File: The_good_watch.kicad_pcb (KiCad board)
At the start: 2 copper layers, 45 x 45 mm, 53 parts, among them IC1 DW01A, J1 Main, J2 USB_C_Receptacle_USB2.0, J3 PROG, J4 Screen, J5 Button, J6 Conn_02x07_Counter_Clockwise, M1 Motor_DC, Q1 FS8205A, Q2 LP0404N3T5G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

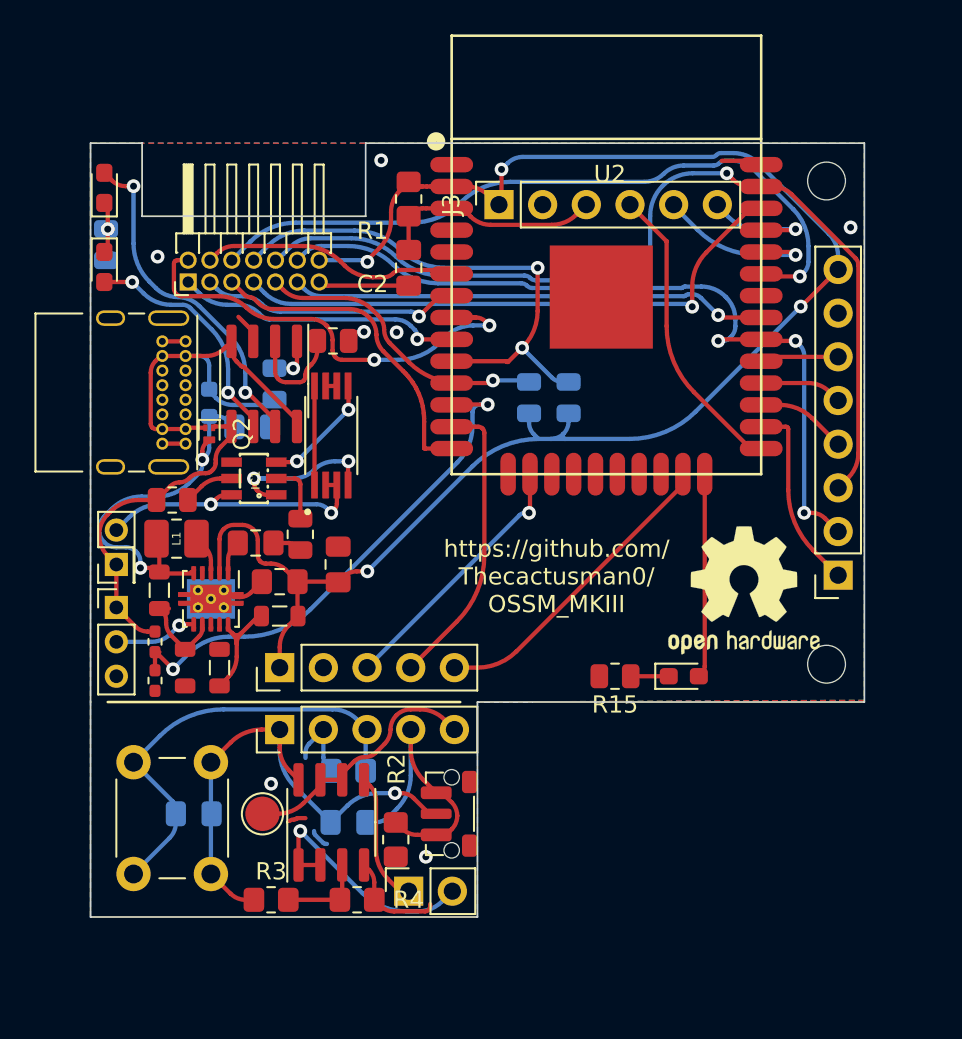
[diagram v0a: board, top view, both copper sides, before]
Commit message: Fixed more connector problems
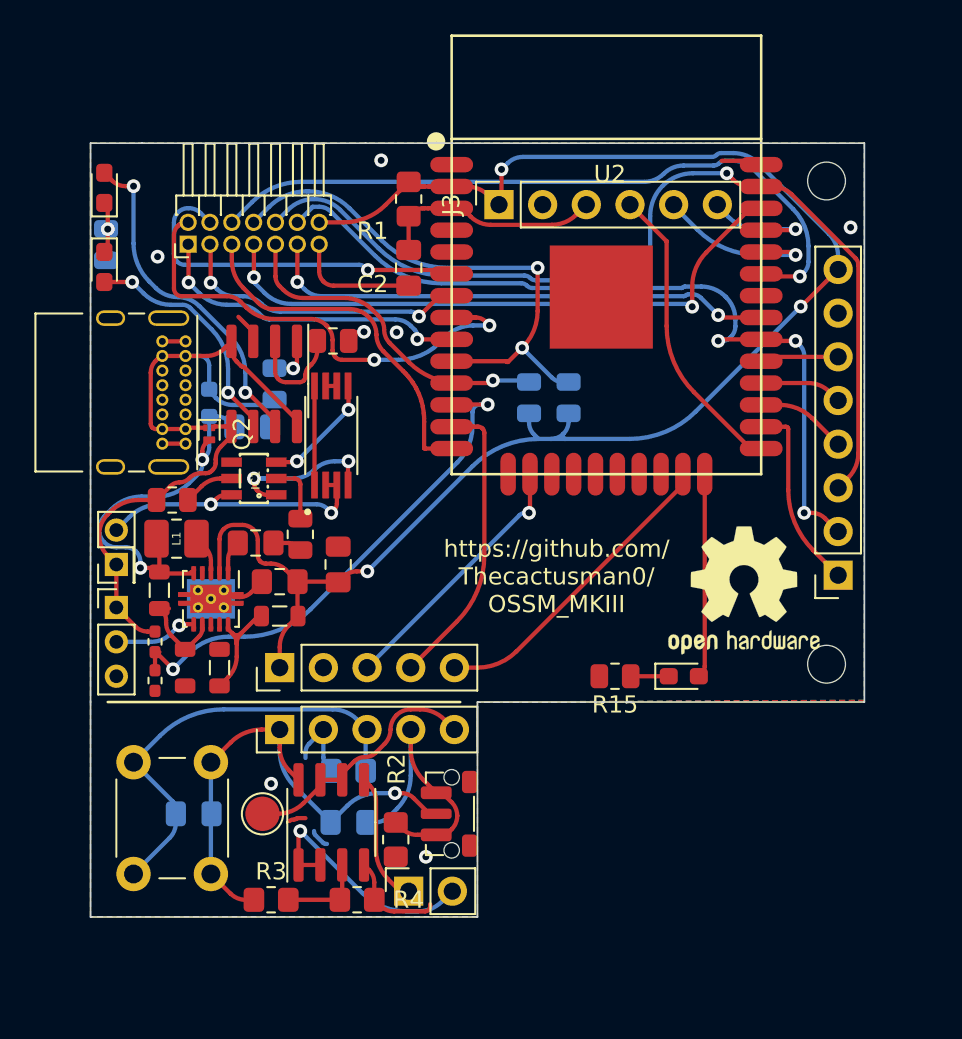
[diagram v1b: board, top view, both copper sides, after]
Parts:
- moved J6 2.20 mm to (105.7, 55.9)
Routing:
- net ANALOG2: track 15.0 -> 21.4 mm, vias 0 -> 1
- net ANALOG1: track 15.1 -> 17.4 mm, vias 1 -> 2
- net SENSE: track 16.7 -> 19.0 mm, vias 1 -> 2
- net MISO: track 27.8 -> 30.0 mm, vias 1 -> 2
- net MGPIO2: track 33.6 -> 35.8 mm, vias 1 -> 2
- net SCL: track 17.3 -> 19.5 mm
- net ANALOG0: track 27.4 -> 29.4 mm
- net GND: track 31.2 -> 33.2 mm
- net MGPIO0: track 18.9 -> 20.8 mm
- net +3V3: track 127.3 -> 125.8 mm, vias 5 -> 4
- net SCK: track 46.4 -> 47.5 mm
- net MOSI: track 55.2 -> 56.2 mm
- net SDA: track 30.4 -> 31.3 mm
- net MGPIO1: track 42.0 -> 41.4 mm
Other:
- outline, holes or cut-outs redrawn

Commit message: Fixed analog pins
encoder pins shut down when wifi enabled now fixed
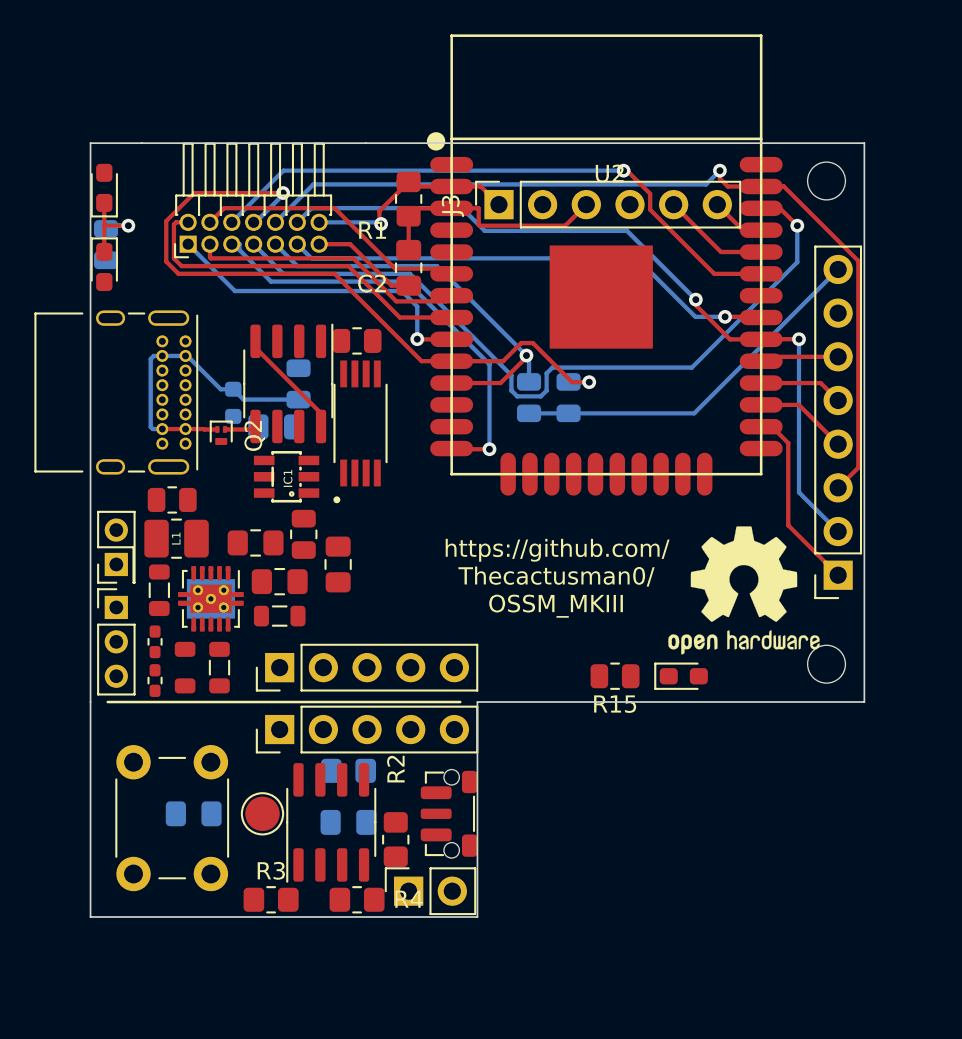
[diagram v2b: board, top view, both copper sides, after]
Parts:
- moved IC1 1.90 mm to (111.4, 69.4)
- moved Q1 1.84 mm to (115.7, 66.3)
- moved R7 1.40 mm to (115.5, 61.5)
- moved U3 1.40 mm to (111.5, 64.0)
- moved C7 1.40 mm to (110.8, 66.5)
- moved D4 1.40 mm to (108.3, 65.1)
- moved R19 1.40 mm to (112.1, 64.0)
- moved Q2 0.71 mm to (107.6, 67.0)
- moved R8 0.20 mm to (112.4, 72.8)
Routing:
- net +3V3: track 125.8 -> 34.6 mm, vias 4 -> 1
- net IO27: track 30.2 -> 0.00 mm, vias 2 -> 0
- net GND: track 33.2 -> 6.20 mm, vias 8 -> 0
- net B2: track 25.8 -> 0.00 mm
- net PSU: track 22.7 -> 0.00 mm, vias 2 -> 0
- net Net-(D2-Pad2): track 19.8 -> 0.00 mm, vias 2 -> 0
- net M_OUT_M: track 18.1 -> 0.00 mm
- net B1_M: track 17.9 -> 0.00 mm
- net +BATT: track 19.7 -> 1.84 mm
- net B1: track 17.4 -> 0.00 mm
- net IO0: track 17.4 -> 0.00 mm
- net -BATT: track 16.9 -> 0.00 mm, vias 2 -> 0
- net B2_M: track 15.4 -> 0.00 mm, vias 1 -> 0
- net M_OUT: track 14.5 -> 0.00 mm
- net Net-(M1-Pad2): track 14.3 -> 0.00 mm, vias 1 -> 0
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- removed copper zone on B.Cu, net GND
- removed copper zone on F.Cu, net GND

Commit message: Added diode protection on usb pwr in and redid layout
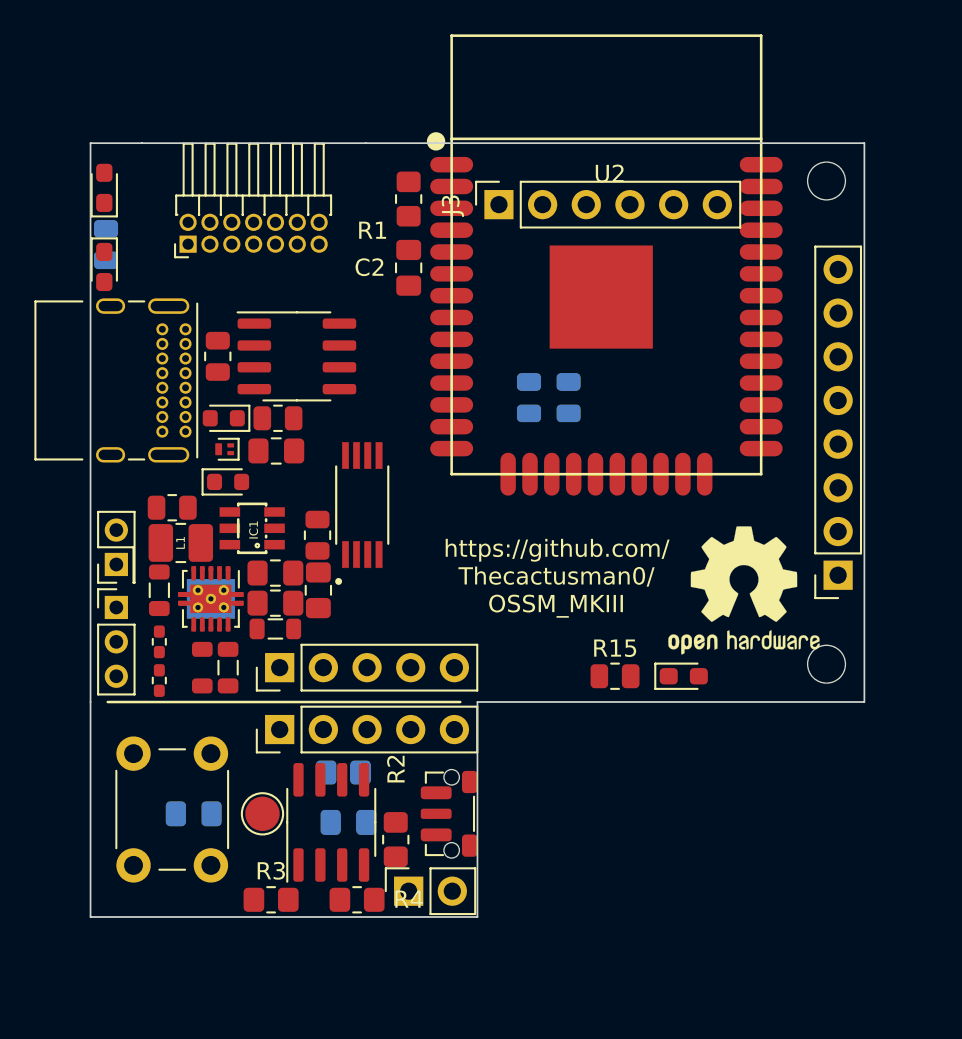
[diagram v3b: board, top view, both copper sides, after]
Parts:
- added D5: D_Schottky, Diode_SMD:D_0603_1608Metric, F.Cu at (107.8, 66.0)
- C7, D4, R19: moved to F.Cu
- moved R7 8.15 mm to (107.4, 62.4), turned to -90 degrees
- moved Q1 4.75 mm to (115.8, 71.0)
- moved D4 4.61 mm to (108.0, 69.7), turned to 0 degrees
- moved IC1 3.61 mm to (109.4, 72.4)
- moved R19 2.33 mm to (110.9, 66.0), turned to 180 degrees
- moved C4 2.09 mm to (110.8, 75.0)
- moved C3 1.89 mm to (113.2, 76.0)
- moved U3 1.68 mm to (112.0, 62.4), turned to 0 degrees
- moved C7 1.40 mm to (110.8, 67.9)
- moved C1 1.27 mm to (110.8, 76.8)
- moved R10 1.00 mm to (106.5, 80.5)
- moved Q2 0.82 mm to (107.8, 67.8), turned to 180 degrees
- moved R8 0.80 mm to (113.2, 72.8)
- moved R11 0.79 mm to (110.8, 78.2)
- moved J2 0.70 mm to (105.5, 60.8)
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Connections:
- J2 pad A4: VCC_IN -> Net-(J2-PadA4)
- J2 pad A9: VCC_IN -> Net-(J2-PadA4)
- J2 pad B4: VCC_IN -> Net-(J2-PadA4)
- J2 pad B9: VCC_IN -> Net-(J2-PadA4)
- J6 pad 2: ANALOG0 -> MGPIO0
- J6 pad 3: ANALOG1 -> MGPIO1
- J6 pad 4: ANALOG2 -> MGPIO2
- J6 pad 5: MGPIO0 -> MGPIO3
- J6 pad 6: MGPIO1 -> MGPIO4
- J6 pad 7: MGPIO2 -> MGPIO5
- U2 pad 13: B1_M -> MGPIO3
- U2 pad 16: B2_M -> MGPIO4
- U2 pad 23: M_OUT_M -> MGPIO5
- U2 pad 6: ANALOG2 -> B1_M
- U2 pad 7: ANALOG1 -> M_OUT_M
- U2 pad 8: ANALOG0 -> B2_M
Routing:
- net MOSI: track 51.3 -> 0.00 mm, vias 1 -> 0
- net SCK: track 45.0 -> 0.00 mm, vias 2 -> 0
- net MGPIO2: track 44.3 -> 0.00 mm, vias 1 -> 0
- net SDA: track 41.9 -> 0.00 mm, vias 2 -> 0
- net MGPIO1: track 35.3 -> 0.00 mm, vias 1 -> 0
- net +3V3: track 34.6 -> 0.00 mm, vias 1 -> 0
- net MISO: track 28.7 -> 0.00 mm, vias 1 -> 0
- net MGPIO0: track 25.2 -> 0.00 mm, vias 1 -> 0
- net VCC_IN: track 24.1 -> 0.00 mm
- net SCL: track 23.9 -> 0.00 mm, vias 1 -> 0
- net ANALOG0: track 20.4 -> 0.00 mm
- net SENSE: track 19.1 -> 0.00 mm, vias 1 -> 0
- net ANALOG1: track 16.0 -> 0.00 mm
- net ANALOG2: track 16.0 -> 0.00 mm
- net EN: track 14.0 -> 0.00 mm
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
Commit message: Layout changes and fuse
Added fuse and fixed mosfet. Not changed on the pcb
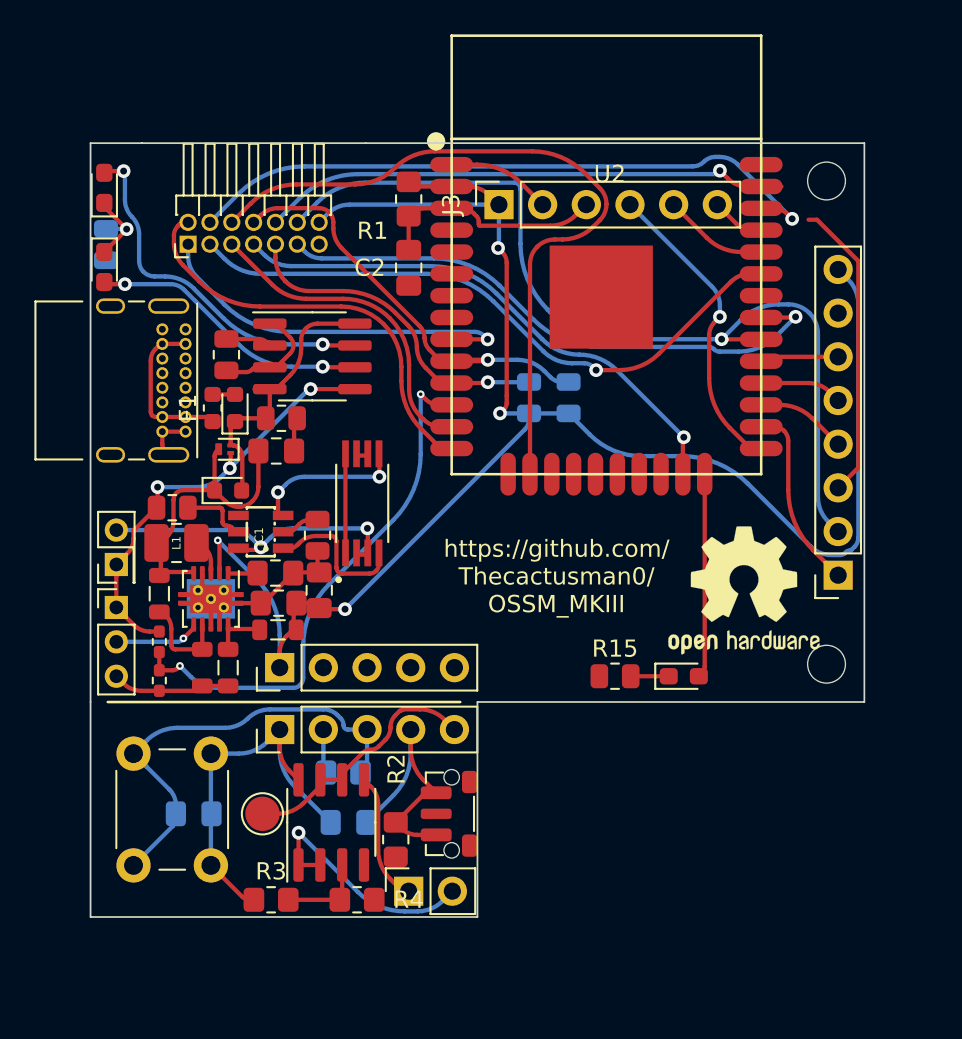
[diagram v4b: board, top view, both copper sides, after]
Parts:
- added F1: PolyFuse, Fuse:Fuse_0603_1608Metric, F.Cu at (107.1, 65.4)
- moved U3 0.90 mm to (112.9, 62.4)
- moved D5 0.88 mm to (108.4, 65.4), turned to 90 degrees
- moved IC1 0.54 mm to (109.9, 72.6)
- moved R7 0.51 mm to (107.9, 62.3)
- moved D4 0.50 mm to (108.0, 70.2)
- moved L1 0.25 mm to (105.0, 73.2)
- moved R9 0.20 mm to (104.0, 76.2)
- moved R19 0.20 mm to (111.1, 66.0)
- moved C1 0.19 mm to (110.9, 76.8)
- moved R11 0.16 mm to (110.9, 78.3)
- moved Q1 0.10 mm to (115.8, 70.9)
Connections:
- D5 pad 2: Net-(J2-PadA4) -> Net-(D5-Pad2)
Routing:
- net +3V3: track 0.00 -> 126.5 mm, vias 0 -> 4
- net SCK: track 0.00 -> 53.6 mm, vias 0 -> 1
- net MOSI: track 0.00 -> 48.4 mm, vias 0 -> 1
- net MGPIO4: track 0.00 -> 42.8 mm
- net MGPIO2: track 0.00 -> 38.5 mm, vias 0 -> 1
- net GND: track 0.00 -> 38.0 mm
- net MGPIO1: track 0.00 -> 36.6 mm, vias 0 -> 1
- net MISO: track 0.00 -> 33.6 mm, vias 0 -> 1
- net MGPIO5: track 0.00 -> 31.2 mm, vias 0 -> 1
- net IO27: track 0.00 -> 31.1 mm, vias 0 -> 2
- net SDA: track 0.00 -> 25.8 mm, vias 0 -> 1
- net B2: track 0.00 -> 25.5 mm
- net MGPIO0: track 0.00 -> 24.7 mm
- net +BATT: track 0.00 -> 24.6 mm, vias 0 -> 3
- net SENSE: track 0.00 -> 22.3 mm, vias 0 -> 1
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
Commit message: Changed power switch
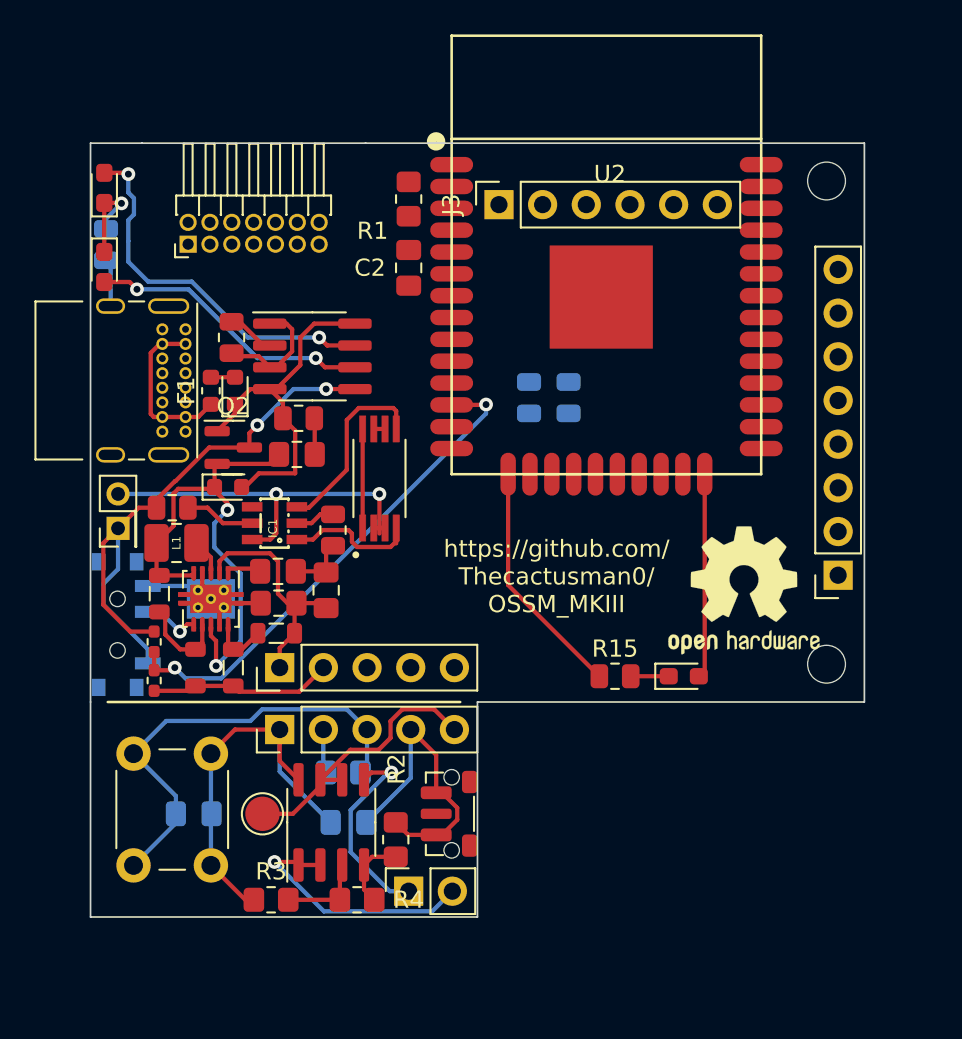
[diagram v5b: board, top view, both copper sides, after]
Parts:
- Q2: value LP0404N3T5G -> DMP6350S-7; footprint Package_TO_SOT_SMD:SOT-883 -> Package_TO_SOT_SMD:SOT-23
- SW3: footprint Connector_PinHeader_2.00mm:PinHeader_1x03_P2.00mm_Vertical -> Button_Switch_SMD:SW_SPDT_PCM12; moved to B.Cu
- moved BT1 2.10 mm to (101.6, 72.4)
- moved Q1 1.76 mm to (116.8, 69.5)
- moved C7 1.22 mm to (112.0, 68.1)
- moved SW3 1.08 mm to (101.9, 78.0), turned to 90 degrees
- moved R7 1.04 mm to (108.2, 61.3)
- moved F1 1.00 mm to (107.0, 64.4)
- moved D5 1.00 mm to (108.4, 64.4)
- moved R19 1.00 mm to (112.1, 66.0)
- moved R8 0.95 mm to (114.1, 72.5)
- moved IC1 0.94 mm to (110.7, 72.1)
- moved Q2 0.51 mm to (108.3, 67.7), turned to 0 degrees
- moved C3 0.40 mm to (113.7, 76.0)
- moved R10 0.40 mm to (106.1, 80.5)
- moved R12 0.30 mm to (108.3, 80.5)
- moved R13 0.30 mm to (103.7, 79.0)
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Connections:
- Q2 pad 1: +BATT -> VCC_IN
- Q2 pad 2: VCC_IN -> PSU
- Q2 pad 3: PSU -> +BATT
- U4 pad 8: GND -> PSU
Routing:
- net +3V3: track 126.5 -> 37.8 mm, vias 4 -> 0
- net SCK: track 53.6 -> 0.00 mm, vias 1 -> 0
- net MOSI: track 48.4 -> 0.00 mm, vias 1 -> 0
- net MGPIO4: track 42.8 -> 0.00 mm
- net MGPIO2: track 38.5 -> 0.00 mm, vias 1 -> 0
- net MGPIO1: track 36.6 -> 0.00 mm, vias 1 -> 0
- net MISO: track 33.6 -> 0.00 mm, vias 1 -> 0
- net MGPIO5: track 31.2 -> 0.00 mm, vias 1 -> 0
- net SDA: track 25.8 -> 0.00 mm, vias 1 -> 0
- net MGPIO0: track 24.7 -> 0.00 mm
- net SENSE: track 22.3 -> 0.00 mm, vias 1 -> 0
- net SCL: track 19.3 -> 0.00 mm, vias 1 -> 0
- net MGPIO3: track 18.8 -> 0.00 mm
- net GND: track 38.0 -> 56.4 mm
- net IO0: track 17.9 -> 0.00 mm, vias 1 -> 0
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
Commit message: Pcb routed
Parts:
- removed REF** (x2): MountingHole_2.2mm_M2, MountingHole:MountingHole_2.2mm_M2
- removed REF**: OSHW-Logo2_9.8x8mm_SilkScreen, Symbol:OSHW-Logo2_9.8x8mm_SilkScreen
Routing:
- net GND: track 56.4 -> 225.8 mm, vias 0 -> 4
- net +3V3: track 37.8 -> 122.7 mm, vias 0 -> 1
- net MOSI: track 0.00 -> 61.1 mm, vias 0 -> 2
- net MGPIO5: track 0.00 -> 60.7 mm, vias 0 -> 5
- net SCK: track 0.00 -> 60.3 mm
- net MGPIO4: track 0.00 -> 54.7 mm, vias 0 -> 4
- net MGPIO1: track 0.00 -> 52.6 mm, vias 0 -> 1
- net SDA: track 0.00 -> 40.3 mm, vias 0 -> 1
- net MGPIO2: track 0.00 -> 39.8 mm, vias 0 -> 1
- net MISO: track 0.00 -> 33.5 mm, vias 0 -> 3
- net B1_M: track 0.00 -> 28.1 mm, vias 0 -> 1
- net B2_M: track 0.00 -> 26.1 mm, vias 0 -> 1
- net M_OUT_M: track 0.00 -> 25.2 mm, vias 0 -> 1
- net MGPIO0: track 0.00 -> 25.0 mm, vias 0 -> 2
- net SCL: track 0.00 -> 21.0 mm, vias 0 -> 1
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- added copper zone on B.Cu, net GND
- added copper zone on F.Cu, net GND
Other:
- board text removed: "https://github.com/ Thecactusman0/ OSSM_MKIII"
